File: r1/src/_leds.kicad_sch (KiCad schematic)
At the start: 13 parts

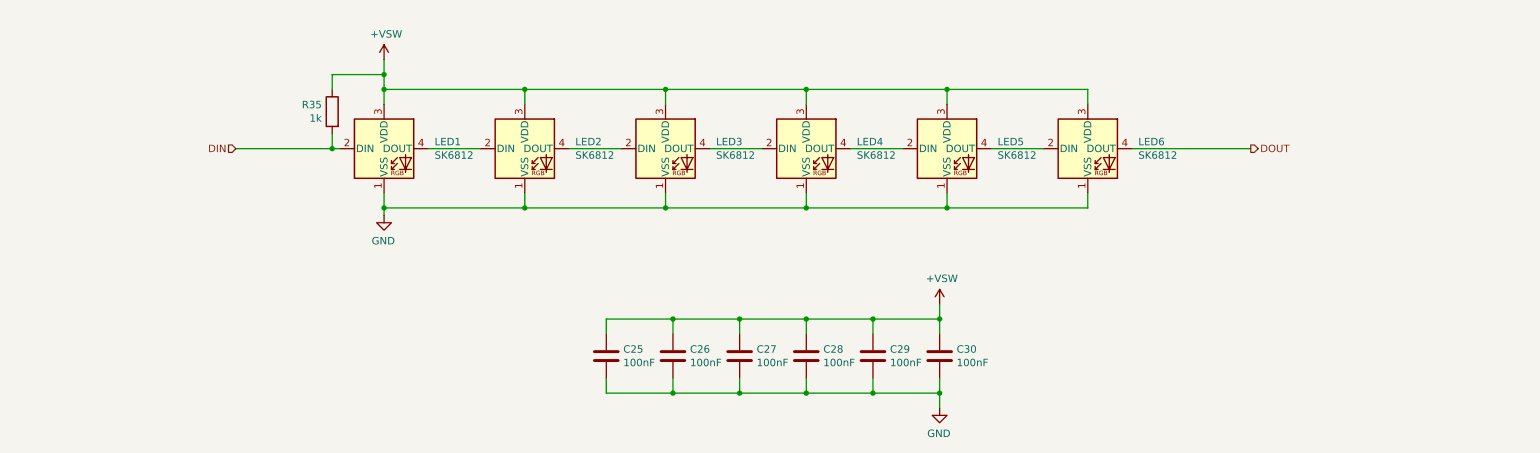
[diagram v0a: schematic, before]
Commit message: Assign MPN's and LCSC part numbers
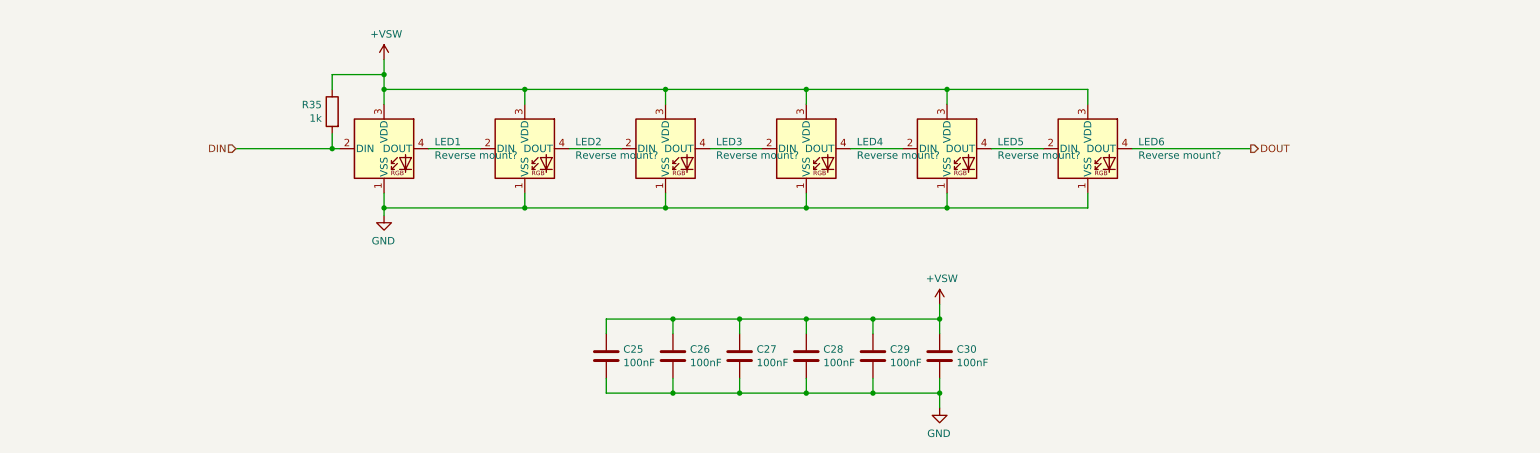
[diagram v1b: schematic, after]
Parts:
- LED1, LED2, LED3, LED4, LED5, LED6: value SK6812 -> Reverse mount?
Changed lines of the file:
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@@
       (effects (font (size 1.27 1.27)) (justify left))
     )
-    (property "Value" "SK6812" (at 92.4814 86.233 0)
+    (property "Value" "Reverse mount?" (at 92.4814 86.233 0)
       (effects (font (size 1.27 1.27)) (justify left))
     )
@@
       (effects (font (size 1.27 1.27)) (justify left))
     )
-    (property "Value" "SK6812" (at 116.6114 86.233 0)
+    (property "Value" "Reverse mount?" (at 116.6114 86.233 0)
       (effects (font (size 1.27 1.27)) (justify left))
     )
@@
       (effects (font (size 1.27 1.27)) (justify left))
     )
-    (property "Value" "SK6812" (at 140.7414 86.233 0)
+    (property "Value" "Reverse mount?" (at 140.7414 86.233 0)
       (effects (font (size 1.27 1.27)) (justify left))
     )
@@
       (effects (font (size 1.27 1.27)) (justify left))
     )
-    (property "Value" "SK6812" (at 164.8714 86.233 0)
+    (property "Value" "Reverse mount?" (at 164.8714 86.233 0)
       (effects (font (size 1.27 1.27)) (justify left))
     )
@@
       (effects (font (size 1.27 1.27)) (justify left))
     )
-    (property "Value" "SK6812" (at 189.0014 86.233 0)
+    (property "Value" "Reverse mount?" (at 189.0014 86.233 0)
       (effects (font (size 1.27 1.27)) (justify left))
     )
@@
       (effects (font (size 1.27 1.27)) (justify left))
     )
-    (property "Value" "SK6812" (at 213.1314 86.233 0)
+    (property "Value" "Reverse mount?" (at 213.1314 86.233 0)
       (effects (font (size 1.27 1.27)) (justify left))
     )

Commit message: Reannotate component refs
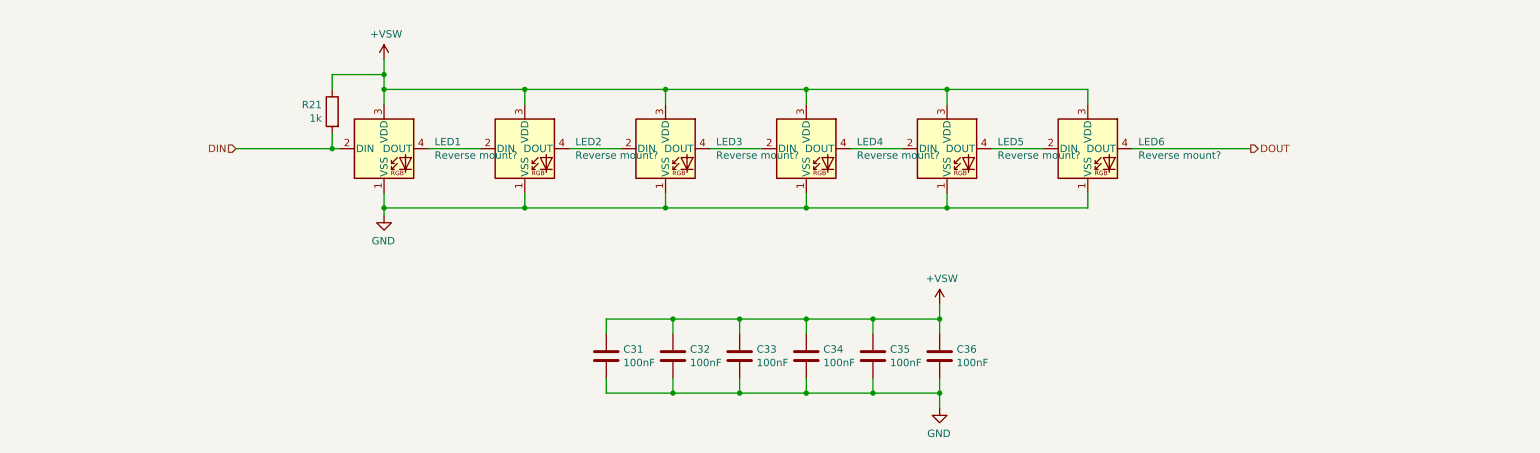
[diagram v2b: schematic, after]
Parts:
- renumbered C25 to C31, C26 to C32, C27 to C33, C28 to C34, C29 to C35, C30 to C36, R35 to R21
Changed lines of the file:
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@@
   (symbol (lib_id "Device:C") (at 121.92 120.65 0) (unit 1)
     (in_bom yes) (on_board yes) (dnp no)
-    (property "Reference" "C25" (at 124.841 119.4816 0)
+    (property "Reference" "C31" (at 124.841 119.4816 0)
       (effects (font (size 1.27 1.27)) (justify left))
     )
@@
       (project "tr23-badge-r1"
         (path "/ab725fe7-4504-40ef-b6af-82d065d00fb6/00000000-0000-0000-0000-00005e660cb6"
-          (reference "C25") (unit 1)
+          (reference "C31") (unit 1)
         )
       )
@@
   (symbol (lib_id "Device:C") (at 133.35 120.65 0) (unit 1)
     (in_bom yes) (on_board yes) (dnp no)
-    (property "Reference" "C26" (at 136.271 119.4816 0)
+    (property "Reference" "C32" (at 136.271 119.4816 0)
       (effects (font (size 1.27 1.27)) (justify left))
     )
@@
       (project "tr23-badge-r1"
         (path "/ab725fe7-4504-40ef-b6af-82d065d00fb6/00000000-0000-0000-0000-00005e660cb6"
-          (reference "C26") (unit 1)
+          (reference "C32") (unit 1)
         )
       )
@@
   (symbol (lib_id "Device:C") (at 144.78 120.65 0) (unit 1)
     (in_bom yes) (on_board yes) (dnp no)
-    (property "Reference" "C27" (at 147.701 119.4816 0)
+    (property "Reference" "C33" (at 147.701 119.4816 0)
       (effects (font (size 1.27 1.27)) (justify left))
     )
@@
       (project "tr23-badge-r1"
         (path "/ab725fe7-4504-40ef-b6af-82d065d00fb6/00000000-0000-0000-0000-00005e660cb6"
-          (reference "C27") (unit 1)
+          (reference "C33") (unit 1)
         )
       )
@@
   (symbol (lib_id "Device:C") (at 156.21 120.65 0) (unit 1)
     (in_bom yes) (on_board yes) (dnp no)
-    (property "Reference" "C28" (at 159.131 119.4816 0)
+    (property "Reference" "C34" (at 159.131 119.4816 0)
       (effects (font (size 1.27 1.27)) (justify left))
     )
@@
       (project "tr23-badge-r1"
         (path "/ab725fe7-4504-40ef-b6af-82d065d00fb6/00000000-0000-0000-0000-00005e660cb6"
-          (reference "C28") (unit 1)
+          (reference "C34") (unit 1)
         )
       )
@@
   (symbol (lib_id "Device:C") (at 167.64 120.65 0) (unit 1)
     (in_bom yes) (on_board yes) (dnp no)
-    (property "Reference" "C29" (at 170.561 119.4816 0)
+    (property "Reference" "C35" (at 170.561 119.4816 0)
       (effects (font (size 1.27 1.27)) (justify left))
     )
@@
       (project "tr23-badge-r1"
         (path "/ab725fe7-4504-40ef-b6af-82d065d00fb6/00000000-0000-0000-0000-00005e660cb6"
-          (reference "C29") (unit 1)
+          (reference "C35") (unit 1)
         )
       )
@@
   (symbol (lib_id "Device:C") (at 179.07 120.65 0) (unit 1)
     (in_bom yes) (on_board yes) (dnp no)
-    (property "Reference" "C30" (at 181.991 119.4816 0)
+    (property "Reference" "C36" (at 181.991 119.4816 0)
       (effects (font (size 1.27 1.27)) (justify left))
     )
@@
       (project "tr23-badge-r1"
         (path "/ab725fe7-4504-40ef-b6af-82d065d00fb6/00000000-0000-0000-0000-00005e660cb6"
-          (reference "C30") (unit 1)
+          (reference "C36") (unit 1)
         )
       )
@@
   (symbol (lib_id "power:+VSW") (at 179.07 111.76 0) (unit 1)
     (in_bom yes) (on_board yes) (dnp no)
-    (property "Reference" "#PWR065" (at 179.07 115.57 0)
+    (property "Reference" "#PWR073" (at 179.07 115.57 0)
       (effects (font (size 1.27 1.27)) hide)
     )
@@
       (project "tr23-badge-r1"
         (path "/ab725fe7-4504-40ef-b6af-82d065d00fb6/00000000-0000-0000-0000-00005e660cb6"
-          (reference "#PWR065") (unit 1)
+          (reference "#PWR073") (unit 1)
         )
       )
@@
   (symbol (lib_id "power:GND") (at 179.07 129.54 0) (mirror y) (unit 1)
     (in_bom yes) (on_board yes) (dnp no)
-    (property "Reference" "#PWR066" (at 179.07 135.89 0)
+    (property "Reference" "#PWR074" (at 179.07 135.89 0)
       (effects (font (size 1.27 1.27)) hide)
     )
@@
       (project "tr23-badge-r1"
         (path "/ab725fe7-4504-40ef-b6af-82d065d00fb6/00000000-0000-0000-0000-00005e660cb6"
-          (reference "#PWR066") (unit 1)
+          (reference "#PWR074") (unit 1)
         )
       )
@@
   (symbol (lib_id "power:GND") (at 83.82 96.52 0) (mirror y) (unit 1)
     (in_bom yes) (on_board yes) (dnp no)
-    (property "Reference" "#PWR064" (at 83.82 102.87 0)
+    (property "Reference" "#PWR072" (at 83.82 102.87 0)
       (effects (font (size 1.27 1.27)) hide)
     )
@@
       (project "tr23-badge-r1"
         (path "/ab725fe7-4504-40ef-b6af-82d065d00fb6/00000000-0000-0000-0000-00005e660cb6"
-          (reference "#PWR064") (unit 1)
+          (reference "#PWR072") (unit 1)
         )
       )
@@
   (symbol (lib_id "Device:R") (at 74.93 78.74 0) (mirror y) (unit 1)
     (in_bom yes) (on_board yes) (dnp no)
-    (property "Reference" "R35" (at 73.152 77.5716 0)
+    (property "Reference" "R21" (at 73.152 77.5716 0)
       (effects (font (size 1.27 1.27)) (justify left))
     )
@@
       (project "tr23-badge-r1"
         (path "/ab725fe7-4504-40ef-b6af-82d065d00fb6/00000000-0000-0000-0000-00005e660cb6"
-          (reference "R35") (unit 1)
+          (reference "R21") (unit 1)
         )
       )
@@
   (symbol (lib_id "power:+VSW") (at 83.82 69.85 0) (unit 1)
     (in_bom yes) (on_board yes) (dnp no)
-    (property "Reference" "#PWR063" (at 83.82 73.66 0)
+    (property "Reference" "#PWR071" (at 83.82 73.66 0)
       (effects (font (size 1.27 1.27)) hide)
     )
@@
       (project "tr23-badge-r1"
         (path "/ab725fe7-4504-40ef-b6af-82d065d00fb6/00000000-0000-0000-0000-00005e660cb6"
-          (reference "#PWR063") (unit 1)
-        )
-      )
+          (reference "#PWR071") (unit 1)
+        )
+      )

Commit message: Change to side-firing LED's
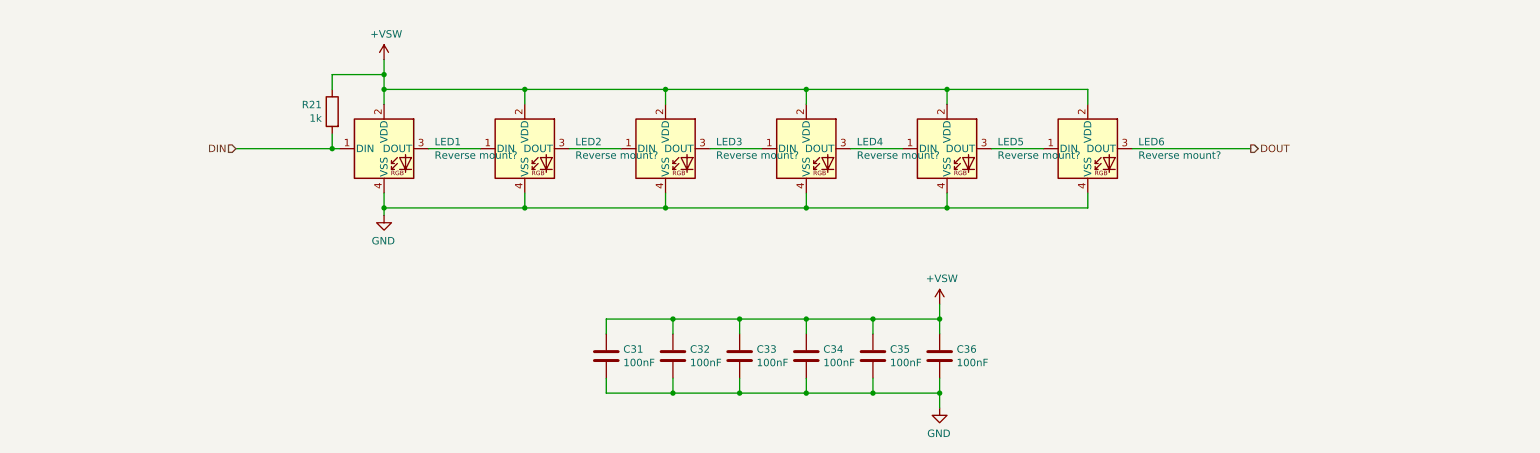
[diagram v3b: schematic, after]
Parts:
- LED1, LED2, LED3, LED4, LED5, LED6: footprint LED_SMD:LED_SK6812_PLCC4_5.0x5.0mm_P3.2mm -> jeffmakes-footprints:LED_SK6812SIDE-A; symbol LED:SK6812 -> j_LED:SK6812SIDE-A
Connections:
- net +VSW: now also LED1.2 (VDD), LED2.2 (VDD), LED3.2 (VDD), LED4.2 (VDD), LED5.2 (VDD), LED6.2 (VDD); no longer LED1.3 (VDD), LED2.3 (VDD), LED3.3 (VDD), LED4.3 (VDD), LED5.3 (VDD), LED6.3 (VDD)
- net DIN: now also LED1.1 (DIN); no longer LED1.2 (DIN)
- net DOUT: now also LED6.3 (DOUT); no longer LED6.4 (DOUT)
- net GND: now also LED1.4 (VSS), LED2.4 (VSS), LED3.4 (VSS), LED4.4 (VSS), LED5.4 (VSS), LED6.4 (VSS); no longer LED1.1 (VSS), LED2.1 (VSS), LED3.1 (VSS), LED4.1 (VSS), LED5.1 (VSS), LED6.1 (VSS)
- new net: LED1.3 (DOUT), LED2.1 (DIN)
- new net: LED2.3 (DOUT), LED3.1 (DIN)
- new net: LED3.3 (DOUT), LED4.1 (DIN)
- new net: LED4.3 (DOUT), LED5.1 (DIN)
- new net: LED5.3 (DOUT), LED6.1 (DIN)
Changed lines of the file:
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@@
     )
   )
-  (symbol (lib_id "LED:SK6812") (at 83.82 85.09 0) (unit 1)
+  (symbol (lib_id "j_LED:SK6812SIDE-A") (at 83.82 85.09 0) (unit 1)
     (in_bom yes) (on_board yes) (dnp no)
     (property "Reference" "LED1" (at 92.4814 83.9216 0)
@@
       (effects (font (size 1.27 1.27)) (justify left))
     )
-    (property "Footprint" "LED_SMD:LED_SK6812_PLCC4_5.0x5.0mm_P3.2mm" (at 85.09 92.71 0)
+    (property "Footprint" "jeffmakes-footprints:LED_SK6812SIDE-A" (at 85.09 92.71 0)
       (effects (font (size 1.27 1.27)) (justify left top) hide)
     )
@@
     )
   )
-  (symbol (lib_id "LED:SK6812") (at 107.95 85.09 0) (unit 1)
+  (symbol (lib_id "j_LED:SK6812SIDE-A") (at 107.95 85.09 0) (unit 1)
     (in_bom yes) (on_board yes) (dnp no)
     (property "Reference" "LED2" (at 116.6114 83.9216 0)
@@
       (effects (font (size 1.27 1.27)) (justify left))
     )
-    (property "Footprint" "LED_SMD:LED_SK6812_PLCC4_5.0x5.0mm_P3.2mm" (at 109.22 92.71 0)
+    (property "Footprint" "jeffmakes-footprints:LED_SK6812SIDE-A" (at 109.22 92.71 0)
       (effects (font (size 1.27 1.27)) (justify left top) hide)
     )
@@
     )
   )
-  (symbol (lib_id "LED:SK6812") (at 132.08 85.09 0) (unit 1)
+  (symbol (lib_id "j_LED:SK6812SIDE-A") (at 132.08 85.09 0) (unit 1)
     (in_bom yes) (on_board yes) (dnp no)
     (property "Reference" "LED3" (at 140.7414 83.9216 0)
@@
       (effects (font (size 1.27 1.27)) (justify left))
     )
-    (property "Footprint" "LED_SMD:LED_SK6812_PLCC4_5.0x5.0mm_P3.2mm" (at 133.35 92.71 0)
+    (property "Footprint" "jeffmakes-footprints:LED_SK6812SIDE-A" (at 133.35 92.71 0)
       (effects (font (size 1.27 1.27)) (justify left top) hide)
     )
@@
     )
   )
-  (symbol (lib_id "LED:SK6812") (at 156.21 85.09 0) (unit 1)
+  (symbol (lib_id "j_LED:SK6812SIDE-A") (at 156.21 85.09 0) (unit 1)
     (in_bom yes) (on_board yes) (dnp no)
     (property "Reference" "LED4" (at 164.8714 83.9216 0)
@@
       (effects (font (size 1.27 1.27)) (justify left))
     )
-    (property "Footprint" "LED_SMD:LED_SK6812_PLCC4_5.0x5.0mm_P3.2mm" (at 157.48 92.71 0)
+    (property "Footprint" "jeffmakes-footprints:LED_SK6812SIDE-A" (at 157.48 92.71 0)
       (effects (font (size 1.27 1.27)) (justify left top) hide)
     )
@@
     )
   )
-  (symbol (lib_id "LED:SK6812") (at 180.34 85.09 0) (unit 1)
+  (symbol (lib_id "j_LED:SK6812SIDE-A") (at 180.34 85.09 0) (unit 1)
     (in_bom yes) (on_board yes) (dnp no)
     (property "Reference" "LED5" (at 189.0014 83.9216 0)
@@
       (effects (font (size 1.27 1.27)) (justify left))
     )
-    (property "Footprint" "LED_SMD:LED_SK6812_PLCC4_5.0x5.0mm_P3.2mm" (at 181.61 92.71 0)
+    (property "Footprint" "jeffmakes-footprints:LED_SK6812SIDE-A" (at 181.61 92.71 0)
       (effects (font (size 1.27 1.27)) (justify left top) hide)
     )
@@
     )
   )
-  (symbol (lib_id "LED:SK6812") (at 204.47 85.09 0) (unit 1)
+  (symbol (lib_id "j_LED:SK6812SIDE-A") (at 204.47 85.09 0) (unit 1)
     (in_bom yes) (on_board yes) (dnp no)
     (property "Reference" "LED6" (at 213.1314 83.9216 0)
@@
       (effects (font (size 1.27 1.27)) (justify left))
     )
-    (property "Footprint" "LED_SMD:LED_SK6812_PLCC4_5.0x5.0mm_P3.2mm" (at 205.74 92.71 0)
+    (property "Footprint" "jeffmakes-footprints:LED_SK6812SIDE-A" (at 205.74 92.71 0)
       (effects (font (size 1.27 1.27)) (justify left top) hide)
     )

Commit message: Schematic for 9 LEDs
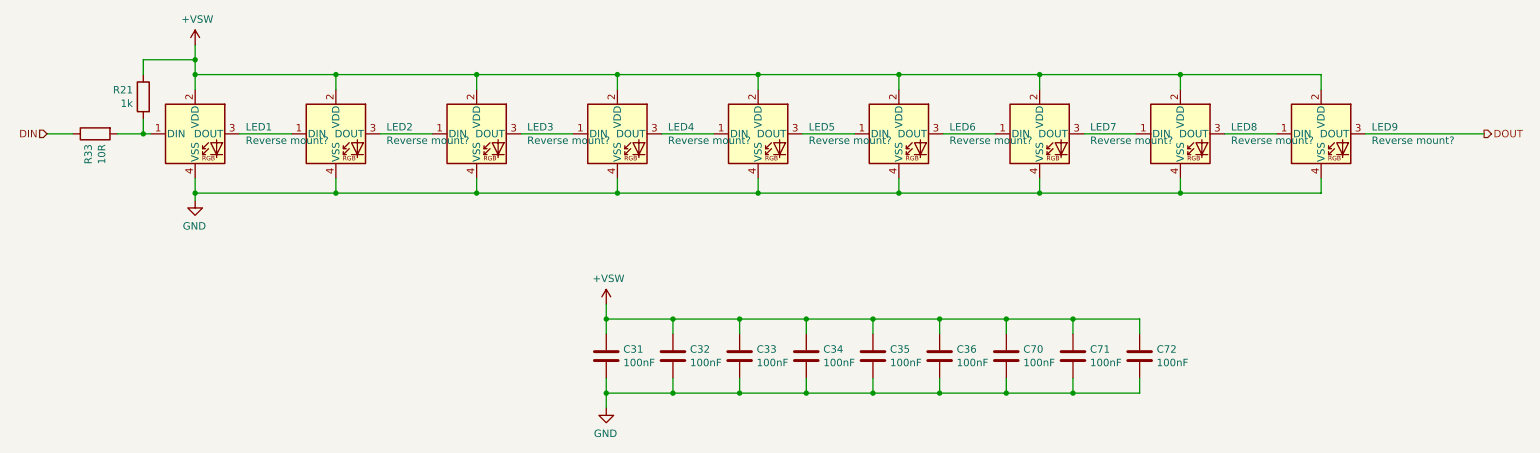
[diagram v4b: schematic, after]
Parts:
- added C70, C71, C72: 100nF, Capacitor_SMD:C_0402_1005Metric, symbol Device:C
- added LED5, LED6, LED7: Reverse mount?, jeffmakes-footprints:LED_SK6812SIDE-A, symbol j_LED:SK6812SIDE-A
- added R33: 10R, Resistor_SMD:R_0402_1005Metric, symbol Device:R
- renumbered LED5 to LED8, LED6 to LED9
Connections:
- net +VSW: now also C70.1, C71.1, C72.1, LED5.2 (VDD), LED6.2 (VDD), LED7.2 (VDD)
- net DIN: now also R33.1; no longer LED1.1 (DIN), R21.2
- net GND: now also C70.2, C71.2, C72.2, LED5.4 (VSS), LED6.4 (VSS), LED7.4 (VSS)
- net at LED4.3 (DOUT): now also LED5.1 (DIN); no longer LED8.1 (DIN)
- new net: LED1.1 (DIN), R21.2, R33.2
- new net: LED7.3 (DOUT), LED8.1 (DIN)
- new net: LED5.3 (DOUT), LED6.1 (DIN)
- new net: LED6.3 (DOUT), LED7.1 (DIN)
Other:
- moved on the sheet: LED1, LED2, LED3, LED4, LED8, LED9, R21
